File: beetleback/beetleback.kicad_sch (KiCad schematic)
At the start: 22 parts, among them J1 Conn_01x05_Female, J3 motor_pad_1, J4 motor_pad_2, Q1 IRF7351TRPBF, Q2 IRF7351TRPBF, U1 ATtiny13A-SS, U2 DRV8701P

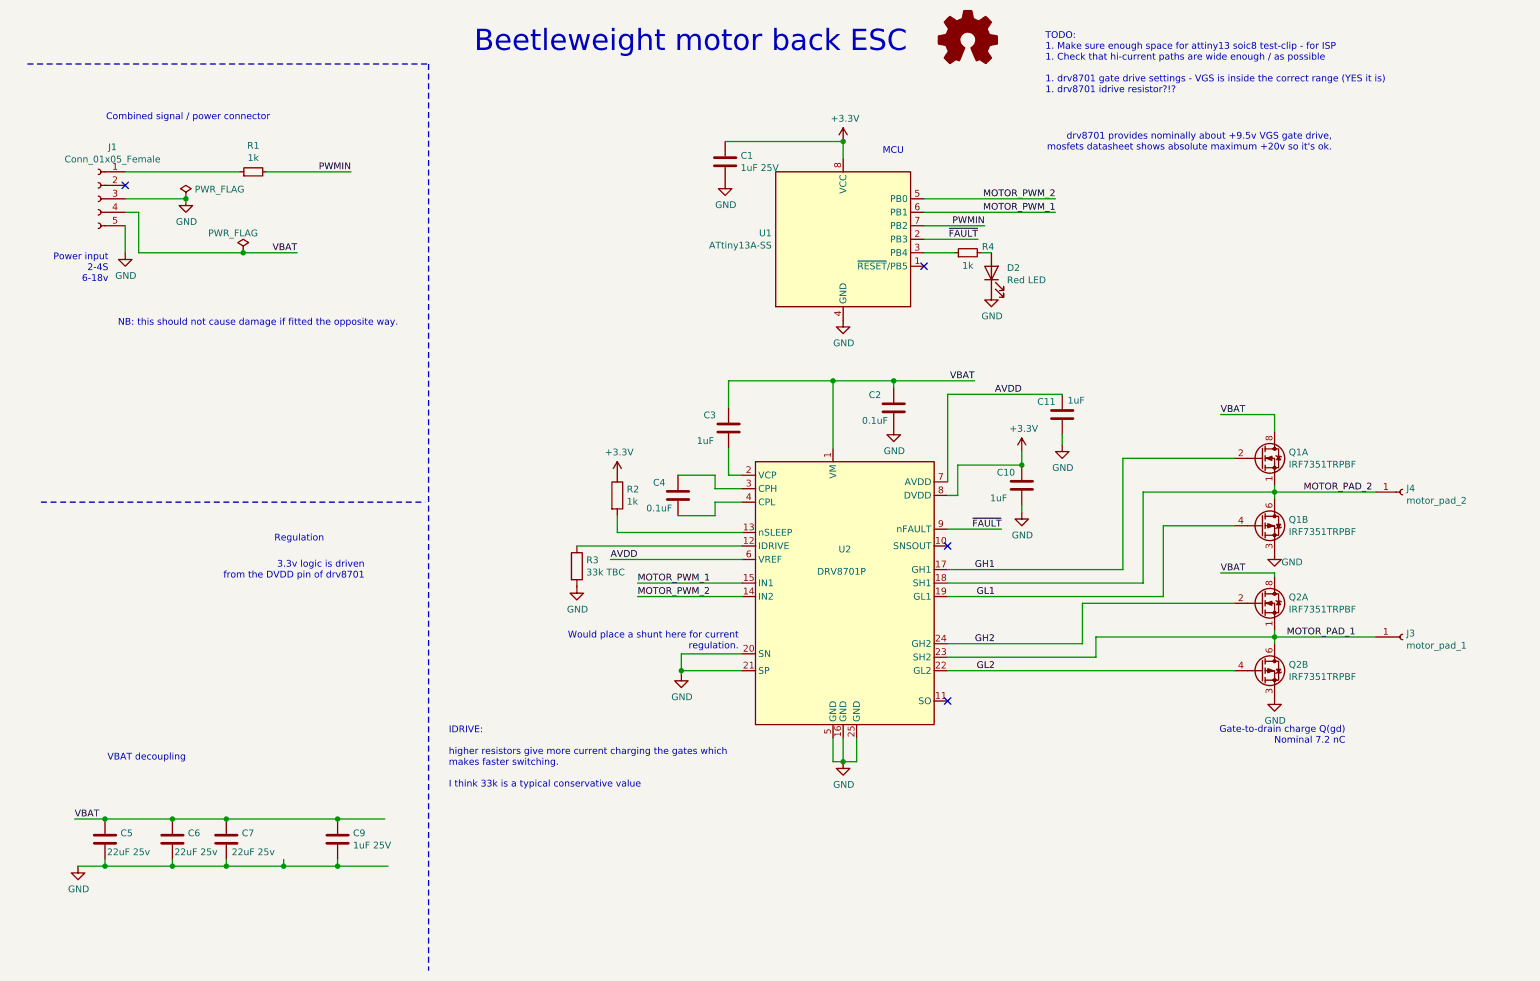
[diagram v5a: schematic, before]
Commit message: identify correct parts, update schematic
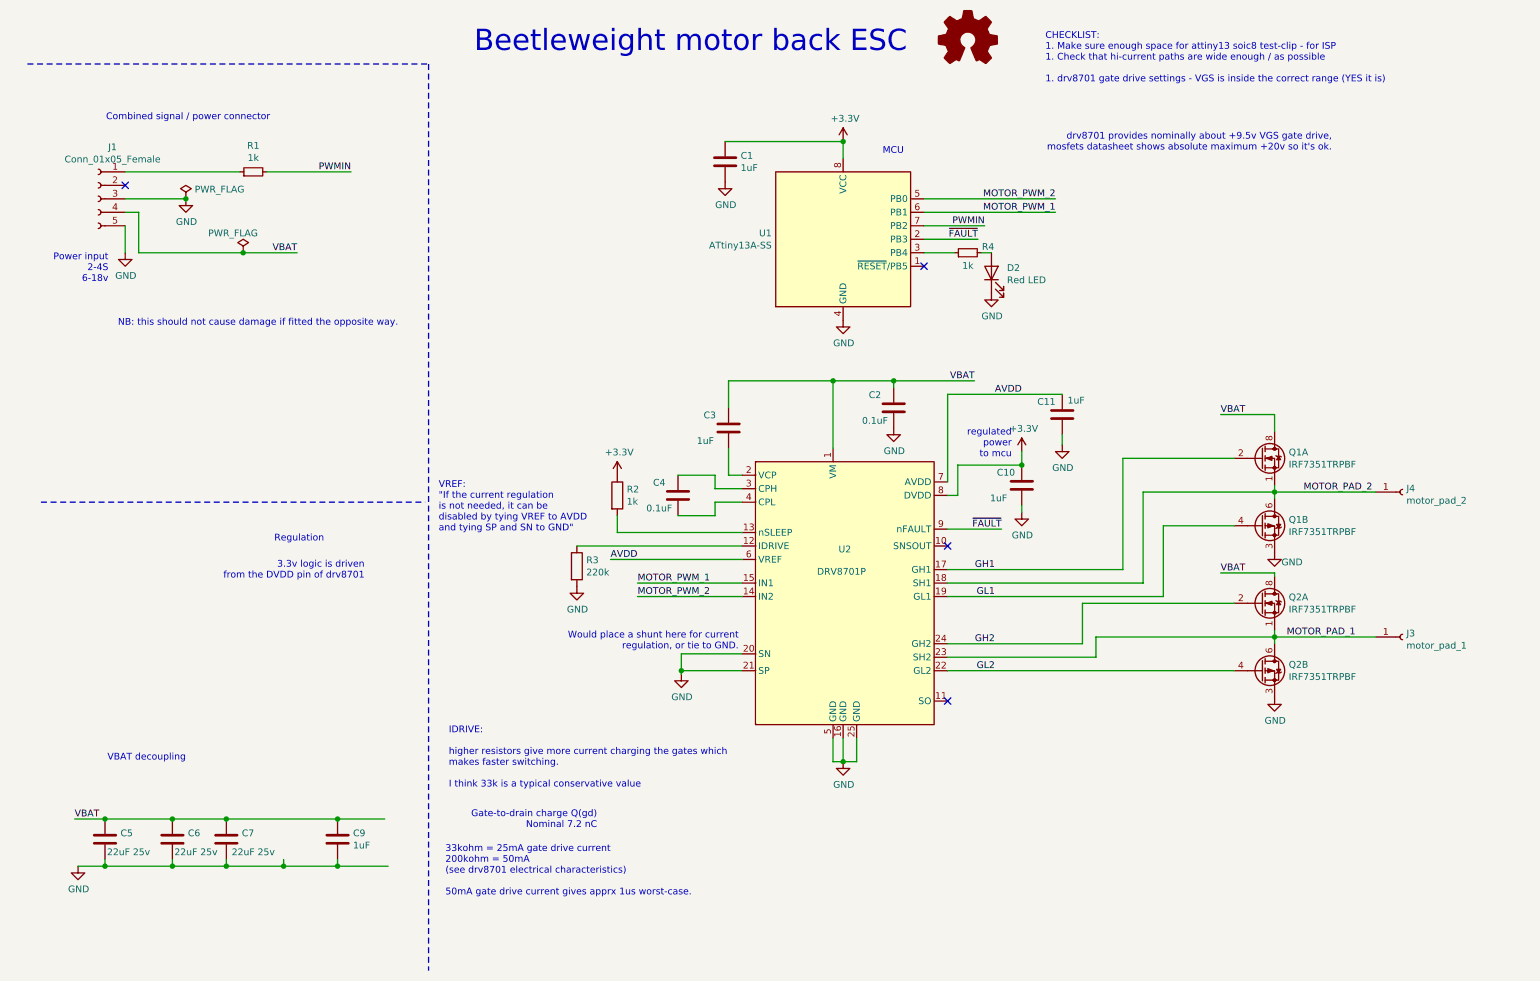
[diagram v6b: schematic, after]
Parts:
- C1, C9: value 1uF 25V -> 1uF
- C10, C11, C3: LCSC (none) -> C52923
- C2, C4: LCSC (none) -> C155422
- J1: LCSC (none) -> C161872
- Q1, Q2: LCSC (none) -> C68403
- R1, R4: LCSC C21190 -> C11702
- R2: LCSC (none) -> C11702
- R3: value 33k TBC -> 220k; LCSC (none) -> C25767
- U2: LCSC (none) -> C114178
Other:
- note added: "33kohm = 25mA gate drive current 200kohm = 50mA (see drv8701 electrical characteristics) 50mA gate drive current gives apprx 1us worst-case."
- note added: "CHECKLIST: 1. Make sure enough space for attiny13 soic8 test-clip - for ISP 1. Check that hi-current paths are wide enough / as possible 1. drv8701 gate drive settings - VGS is inside the correct range (YES it is)"
- note added: "VREF: "If the current regulation is not needed, it can be disabled by tying VREF to AVDD and tying SP and SN to GND""
- note added: "Would place a shunt here for current regulation, or tie to GND."
- note added: "regulated power to mcu"
- note removed: "TODO: 1. Make sure enough space for attiny13 soic8 test-clip - for ISP 1. Check that hi-current paths are wide enough / as possible 1. drv8701 gate drive settings - VGS is inside the correct range (YES it is) 1. drv8701 idrive resistor?!?"
- note removed: "Would place a shunt here for current regulation."
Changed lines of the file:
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@@
   (junction (at 244.475 108.585) (diameter 1.016) (color 0 0 0 0))
   (junction (at 244.475 135.89) (diameter 1.016) (color 0 0 0 0))
+  (no_connect (at 182.88 118.745))
+  (no_connect (at 27.94 50.8))
   (no_connect (at 182.88 147.955))
-  (no_connect (at 182.88 118.745))
   (no_connect (at 178.435 66.04))
-  (no_connect (at 27.94 50.8))
   (wire (pts (xy 18.415 170.18) (xy 24.13 170.18))
     (stroke (width 0) (type solid) (color 0 0 0 0))
@@
     (at 79.375 77.47 0)
     (effects (font (size 1.27 1.27)) (justify right bottom))
+  )
+  (text "VREF: \n\"If the current regulation\nis not needed, it can be\ndisabled by tying VREF to AVDD\nand tying SP and SN to GND\""
+    (at 86.995 116.205 0)
+    (effects (font (size 1.27 1.27)) (justify left bottom))
+  )
+  (text "33kohm = 25mA gate drive current\n200kohm = 50mA\n(see drv8701 electrical characteristics)\n\n50mA gate drive current gives apprx 1us worst-case."
+    (at 88.265 184.785 0)
+    (effects (font (size 1.27 1.27)) (justify left bottom))
   )
   (text "IDRIVE:\n\nhigher resistors give more current charging the gates which\nmakes faster switching.\n\nI think 33k is a typical conservative value"
@@
     (effects (font (size 1.27 1.27)) (justify left bottom))
   )
-  (text "Would place a shunt here for current\nregulation." (at 143.51 138.43 180)
+  (text "Gate-to-drain charge Q(gd)\nNominal 7.2 nC\n" (at 116.84 172.085 180)
+    (effects (font (size 1.27 1.27)) (justify right bottom))
+  )
+  (text "Would place a shunt here for current\nregulation, or tie to GND."
+    (at 143.51 138.43 0)
     (effects (font (size 1.27 1.27)) (justify right bottom))
   )
@@
     (effects (font (size 4 4)) (justify right bottom))
   )
-  (text "TODO:\n1. Make sure enough space for attiny13 soic8 test-clip - for ISP\n1. Check that hi-current paths are wide enough / as possible\n\n1. drv8701 gate drive settings - VGS is inside the correct range (YES it is)\n1. drv8701 idrive resistor?!?\n"
+  (text "regulated \npower\nto mcu" (at 194.945 102.235 180)
+    (effects (font (size 1.27 1.27)) (justify right bottom))
+  )
+  (text "CHECKLIST:\n1. Make sure enough space for attiny13 soic8 test-clip - for ISP\n1. Check that hi-current paths are wide enough / as possible\n\n1. drv8701 gate drive settings - VGS is inside the correct range (YES it is)\n\n"
     (at 201.295 33.655 0)
     (effects (font (size 1.27 1.27)) (justify left bottom))
@@
   (text "drv8701 provides nominally about +9.5v VGS gate drive,\nmosfets datasheet shows absolute maximum +20v so it's ok."
     (at 255.27 44.45 0)
-    (effects (font (size 1.27 1.27)) (justify right bottom))
-  )
-  (text "Gate-to-drain charge Q(gd)\nNominal 7.2 nC\n" (at 257.81 156.21 180)
     (effects (font (size 1.27 1.27)) (justify right bottom))
   )
@@
       (effects (font (size 1.27 1.27)) hide)
     )
-    (property "LCSC" "C21190" (id 4) (at 52.07 48.26 0)
+    (property "LCSC" "C11702" (id 4) (at 52.07 48.26 0)
       (effects (font (size 1.27 1.27)) hide)
     )
@@
       (effects (font (size 1.27 1.27)) hide)
     )
-    (property "LCSC" "C21190" (id 4) (at 186.69 63.5 0)
+    (property "LCSC" "C11702" (id 4) (at 186.69 63.5 0)
       (effects (font (size 1.27 1.27)) hide)
     )
@@
       (effects (font (size 1.27 1.27)) (justify left))
     )
-    (property "Value" "33k TBC" (id 1) (at 114.808 123.704 0)
+    (property "Value" "220k" (id 1) (at 114.808 123.704 0)
       (effects (font (size 1.27 1.27)) (justify left))
     )
@@
       (effects (font (size 1.27 1.27)) hide)
     )
+    (property "LCSC" "C25767" (id 4) (at 113.03 122.555 0)
+      (effects (font (size 1.27 1.27)) hide)
+    )
   )
   (symbol (lib_id "Device:R") (at 120.65 109.22 0) (unit 1)
@@
     )
     (property "Datasheet" "~" (id 3) (at 120.65 109.22 0)
+      (effects (font (size 1.27 1.27)) hide)
+    )
+    (property "LCSC" "C11702" (id 4) (at 120.65 109.22 0)
       (effects (font (size 1.27 1.27)) hide)
     )
@@
       (effects (font (size 1.27 1.27)) (justify left))
     )
-    (property "Value" "1uF 25V" (id 1) (at 70.8661 175.1393 0)
+    (property "Value" "1uF" (id 1) (at 70.8661 175.1393 0)
       (effects (font (size 1.27 1.27)) (justify left))
     )
@@
       (effects (font (size 1.27 1.27)) hide)
     )
+    (property "LCSC" "C155422" (id 4) (at 132.08 109.22 0)
+      (effects (font (size 1.27 1.27)) hide)
+    )
   )
   (symbol (lib_id "Device:C") (at 140.97 46.355 0) (unit 1)
@@
       (effects (font (size 1.27 1.27)) (justify left))
     )
-    (property "Value" "1uF 25V" (id 1) (at 143.8911 47.5043 0)
+    (property "Value" "1uF" (id 1) (at 143.8911 47.5043 0)
       (effects (font (size 1.27 1.27)) (justify left))
     )
@@
       (effects (font (size 1.27 1.27)) hide)
     )
+    (property "LCSC" "C52923" (id 4) (at 141.605 96.52 0)
+      (effects (font (size 1.27 1.27)) hide)
+    )
   )
   (symbol (lib_id "Device:C") (at 172.72 92.71 0) (unit 1)
@@
       (effects (font (size 1.27 1.27)) hide)
     )
+    (property "LCSC" "C155422" (id 4) (at 172.72 92.71 0)
+      (effects (font (size 1.27 1.27)) hide)
+    )
   )
   (symbol (lib_id "Device:C") (at 196.85 107.315 0) (unit 1)
@@
       (effects (font (size 1.27 1.27)) hide)
     )
+    (property "LCSC" "C52923" (id 4) (at 196.85 107.315 0)
+      (effects (font (size 1.27 1.27)) hide)
+    )
   )
   (symbol (lib_id "Device:C") (at 204.47 93.98 0) (unit 1)
@@
     )
     (property "Datasheet" "~" (id 3) (at 204.47 93.98 0)
+      (effects (font (size 1.27 1.27)) hide)
+    )
+    (property "LCSC" "C52923" (id 4) (at 204.47 93.98 0)
       (effects (font (size 1.27 1.27)) hide)
     )
@@
       (effects (font (size 1.27 1.27)) hide)
     )
+    (property "LCSC" "C161872" (id 4) (at 22.86 53.34 0)
+      (effects (font (size 1.27 1.27)) hide)
+    )
   )
   (symbol (lib_id "Transistor_FET:IRF7343PBF") (at 241.935 102.235 0) (unit 1)
@@
       (effects (font (size 1.27 1.27)) (justify left) hide)
     )
+    (property "LCSC" "C68403" (id 4) (at 241.935 102.235 0)
+      (effects (font (size 1.27 1.27)) hide)
+    )
   )
   (symbol (lib_id "Transistor_FET:IRF7343PBF") (at 241.935 114.935 0) (unit 2)
@@
       (effects (font (size 1.27 1.27)) (justify left) hide)
     )
+    (property "LCSC" "C68403" (id 4) (at 241.935 114.935 0)
+      (effects (font (size 1.27 1.27)) hide)
+    )
   )
   (symbol (lib_id "Transistor_FET:IRF7343PBF") (at 241.935 129.54 0) (unit 1)
@@
       (effects (font (size 1.27 1.27)) (justify left) hide)
     )
+    (property "LCSC" "C68403" (id 4) (at 241.935 129.54 0)
+      (effects (font (size 1.27 1.27)) hide)
+    )
   )
   (symbol (lib_id "Transistor_FET:IRF7343PBF") (at 241.935 142.24 0) (unit 2)
@@
     (property "Datasheet" "http://www.irf.com/product-info/datasheets/data/irf7343ipbf.pdf" (id 3) (at 244.475 142.24 0)
       (effects (font (size 1.27 1.27)) (justify left) hide)
+    )
+    (property "LCSC" "C68403" (id 4) (at 241.935 142.24 0)
+      (effects (font (size 1.27 1.27)) hide)
     )
   )
@@
       (effects (font (size 1.27 1.27)) hide)
     )
+    (property "LCSC" "C114178" (id 4) (at 165.1 134.62 0)
+      (effects (font (size 1.27 1.27)) hide)
+    )
   )
   (sheet_instances
@@
     )
     (path "/61cff6ee-74aa-40de-b883-f20a48570774"
-      (reference "C1") (unit 1) (value "1uF 25V") (footprint "Capacitor_SMD:C_0402_1005Metric")
+      (reference "C1") (unit 1) (value "1uF") (footprint "Capacitor_SMD:C_0402_1005Metric")
     )
     (path "/a39b1e3b-94c7-42eb-a685-4e6eac56a76e"
@@
     )
     (path "/e3151301-bd2c-4afe-9ee4-ba1a357ed263"
-      (reference "C9") (unit 1) (value "1uF 25V") (footprint "Capacitor_SMD:C_0402_1005Metric")
+      (reference "C9") (unit 1) (value "1uF") (footprint "Capacitor_SMD:C_0402_1005Metric")
     )
     (path "/f3ea6508-a692-493a-b295-a738bc910c0f"
@@
     )
     (path "/96fca56c-a1c6-47bb-9c21-6e480b894a8c"
-      (reference "R3") (unit 1) (value "33k TBC") (footprint "Resistor_SMD:R_0402_1005Metric")
+      (reference "R3") (unit 1) (value "220k") (footprint "Resistor_SMD:R_0402_1005Metric")
     )
     (path "/1f054975-e5a8-442f-b188-82daf3387f2d"
